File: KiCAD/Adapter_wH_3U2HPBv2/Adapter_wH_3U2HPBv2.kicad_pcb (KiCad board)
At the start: 2 copper layers, 9.8 x 128.5 mm, 3 parts

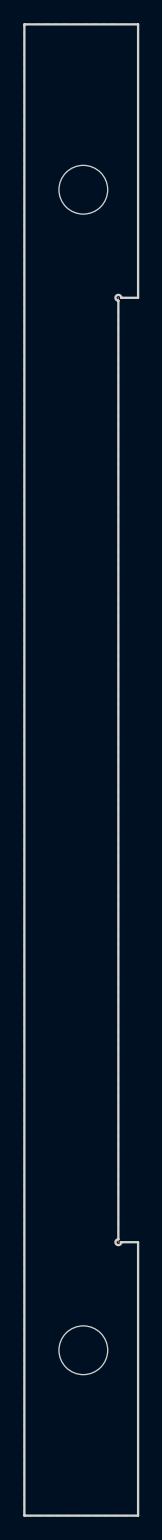
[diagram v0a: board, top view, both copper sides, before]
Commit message: updated all modules to use plated through-holes wherever possible
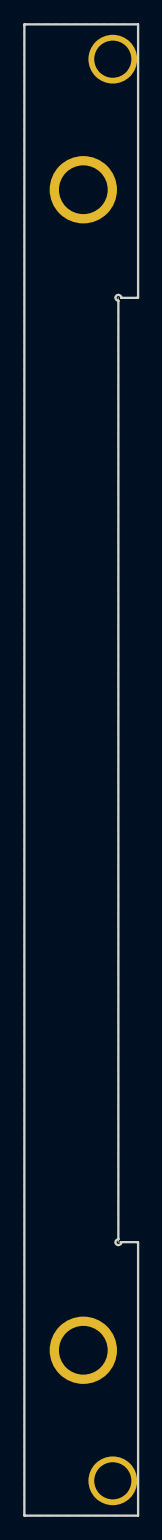
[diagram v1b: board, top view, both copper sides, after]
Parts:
- moved H1 2.54 mm to (7.62, 5.42)
- moved H2 2.54 mm to (7.62, 127.9)
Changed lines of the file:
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@@
 	(footprint "EXC:MountingHole_3.2mm_M3"
 		(layer "F.Cu")
-		(at 5.08 127.925)
+		(at 7.62 127.925)
 		(descr "Mounting Hole 3.2mm, no annular, M3")
 		(tags "mounting hole 3.2mm no annular m3")
@@
 			)
 		)
-		(pad "" np_thru_hole oval
+		(pad "" thru_hole circle
 			(at 0 0)
-			(size 4.34 3.2)
-			(drill oval 4.34 3.2)
+			(size 4.2 4.2)
+			(drill 3.2)
 			(layers "*.Cu" "*.Mask")
+			(remove_unused_layers no)
 		)
 		(embedded_fonts no)
@@
 			)
 		)
-		(pad "" np_thru_hole circle
+		(pad "" thru_hole circle
 			(at 0 0)
-			(size 4.2 4.2)
+			(size 5.8 5.8)
 			(drill 4.2)
 			(layers "*.Cu" "*.Mask")
-		)
-		(pad "" np_thru_hole circle
+			(remove_unused_layers no)
+		)
+		(pad "" thru_hole circle
 			(at 0 100)
-			(size 4.2 4.2)
+			(size 5.8 5.8)
 			(drill 4.2)
 			(layers "*.Cu" "*.Mask")
+			(remove_unused_layers no)
 		)
 		(embedded_fonts no)
@@
 	(footprint "EXC:MountingHole_3.2mm_M3"
 		(layer "F.Cu")
-		(at 5.08 5.425)
+		(at 7.62 5.425)
 		(descr "Mounting Hole 3.2mm, no annular, M3")
 		(tags "mounting hole 3.2mm no annular m3")
@@
 			)
 		)
-		(pad "" np_thru_hole oval
+		(pad "" thru_hole circle
 			(at 0 0)
-			(size 4.34 3.2)
-			(drill oval 4.34 3.2)
+			(size 4.2 4.2)
+			(drill 3.2)
 			(layers "*.Cu" "*.Mask")
+			(remove_unused_layers no)
 		)
 		(embedded_fonts no)
